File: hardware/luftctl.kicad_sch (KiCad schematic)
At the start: 41 parts, among them J1 USB_C_Receptacle_USB2.0, J2 UART, J3 I2C, J4 PWM Fan, J5 PWM Fan, SW1 Reset, U1 LMR62014XMF, U2 MIC5504-3.3YM5, U3 USBLC6-4SC6, U4 ESP32-C3-WROOM-02

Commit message: Add USB-C PD 12V input + GPIO breakout header (routed board + fab files)
Two hardware modifications to luftctl:

1. Power the fans from 12V negotiated over USB-C Power Delivery instead of
   boosting 5V on-board. Removes the boost (U1 LMR62014), its inductor,
   Schottky, feedback divider and the 5.1k CC pull-downs; adds a CH224K PD
   trigger (U5) and an LMR51420 buck (U6, 12V->3V3) for logic. The +5V rail is
   merged into +12V and the J2/J3 connector power pins move to +3V3.
2. Break out spare GPIOs on a 2.54mm Dupont header (J6): IO2, IO3 (freed from
   the removed 12V-enable), IO8, UART TX/RX, plus 3V3 and GND.

Schematic (luftctl.kicad_sch) updated and netlist-verified. A fully placed and
autorouted board is provided as luftctl-modified.kicad_pcb (board enlarged for
the new section + header; solid B.Cu ground plane; 0 unrouted, 0 clearance
violations). Firmware (main.py, esphome/luftctl.yaml) drops the 12V-enable.

JLCPCB assembly outputs (gerbers, drill, BOM, rotation-corrected CPL) for both
the original and modified boards are in hardware/jlcpcb/, with parts verified
in-stock against the jlcparts database. See hardware/MODIFICATIONS.md for the
full change spec, part selection, and the datasheet values still to confirm
(CH224K CFG straps for 12V; buck feedback divider).

Co-Authored-By: Claude Opus 4.8 (1M context) <noreply@anthropic.com>
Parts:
- removed C6: 220pF, Capacitor_SMD:C_0805_2012Metric_Pad1.18x1.45mm_HandSolder, symbol Device:C_Small
- removed D1: 1N5819, Diode_SMD:D_SOD-123, symbol Device:D_Schottky_Small
- removed L1: 10µH, Inductor_SMD:L_Bourns_SRN6045TA, symbol Device:L_Small
- removed R1: 113kΩ, Resistor_SMD:R_0805_2012Metric_Pad1.20x1.40mm_HandSolder, symbol Device:R_Small
- removed R2: 13kΩ, Resistor_SMD:R_0805_2012Metric_Pad1.20x1.40mm_HandSolder, symbol Device:R_Small
- removed R4, R5: 5.1kΩ, Resistor_SMD:R_0805_2012Metric_Pad1.20x1.40mm_HandSolder, symbol Device:R_Small
- removed U1: LMR62014XMF, Package_TO_SOT_SMD:SOT-23-5, symbol Regulator_Switching:LMR62014XMF
- removed U2: MIC5504-3.3YM5, Package_TO_SOT_SMD:SOT-23-5, symbol Regulator_Linear:MIC5504-3.3YM5
- added C12: 100nF, Capacitor_SMD:C_0805_2012Metric_Pad1.18x1.45mm_HandSolder, symbol Device:C_Small
- added C13: 10µF, Capacitor_SMD:C_0805_2012Metric_Pad1.18x1.45mm_HandSolder, symbol Device:C_Small
- added C14: 22µF, Capacitor_SMD:C_0805_2012Metric_Pad1.18x1.45mm_HandSolder, symbol Device:C_Small
- added C15: 1µF, Capacitor_SMD:C_0805_2012Metric_Pad1.18x1.45mm_HandSolder, symbol Device:C_Small
- added J6: Conn_01x08, Connector_PinHeader_2.54mm:PinHeader_1x08_P2.54mm_Vertical, symbol Connector_Generic:Conn_01x08
- added L2: 10µH, Inductor_SMD:L_Bourns_SRN6045TA, symbol Device:L_Small
- added R11: 100kΩ, Resistor_SMD:R_0805_2012Metric_Pad1.20x1.40mm_HandSolder, symbol Device:R_Small
- added R12: 22kΩ, Resistor_SMD:R_0805_2012Metric_Pad1.20x1.40mm_HandSolder, symbol Device:R_Small
- added R13, R14, R15: 0Ω, Resistor_SMD:R_0805_2012Metric_Pad1.20x1.40mm_HandSolder, symbol Device:R_Small
- added U5: CH224K, Package_SO:SSOP-10-1EP_3.9x4.9mm_P1mm_EP2.1x3.3mm, symbol Interface_USB:CH224K
- added U6: LMR51420YFDDCR, Package_TO_SOT_SMD:SOT-23-6, symbol Regulator_Switching:LMR51430
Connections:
- net +12V: now also C1.2, C3.2, C5.2, C7.2, FB1.2, TP2.1, C13.1, U6.3 (VIN), U6.5 (EN)
- net +3V3: now also J2.2 (Pin_2), J3.2 (Pin_2), C14.1, J6.1 (Pin_1), L2.2, R11.1
- net CC1: now also U5.7 (CC1)
- net CC2: now also U5.6 (CC2)
- net GND: now also C13.2, C14.2, C15.2, J6.2 (Pin_2), J6.8 (Pin_8), R12.2, R13.2, R14.2, R15.2, U5.11 (GND), U6.1 (GND)
- net GPIO2: now also J6.3 (Pin_3)
- net GPIO8: now also J6.5 (Pin_5)
- net RXD: now also J6.6 (Pin_6)
- net TXD: now also J6.7 (Pin_7)
- net VBUS: now also U5.8 (VBUS)
- removed net +5V: C1.2, C3.2, C5.2, C7.2, FB1.2, J2.2 (Pin_2), J3.2 (Pin_2), TP2.1
- net 12V_EN renamed GPIO3
- net GPIO3: now also J6.4 (Pin_4)
- new net BST_BUCK: C12.1, U6.6 (CB)
- new net CFG1: R13.1, U5.9 (CFG1)
- new net CFG2: R14.1, U5.2 (CFG2)
- new net CFG3: R15.1, U5.3 (CFG3)
- new net FB_BUCK: R11.2, R12.1, U6.4 (FB)
- new net SW_BUCK: C12.2, L2.1, U6.2 (SW)
- new net VDD_CH: C15.1, U5.1 (VDD)
- no-connect marks 2 -> 5

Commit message: CH224K: fix 12V CFG straps + VDD supply per datasheet; re-route
Datasheet research (WCH CH224 V2.0; TI LMR51420 SLUSEF6C), cross-verified,
corrected two bugs in the CH224K PD-trigger wiring that would have made the
board negotiate 9V with an unpowered controller:

- CFG3 must be pulled HIGH (to VDD) for 12V, not strapped to GND. CH224K has no
  internal CFG pull-ups, so R15 is changed from a 0R GND strap to a 10k pull-up
  to VDD (R15/CFG3 -> VDD_CH). CFG1/CFG2 stay strapped to GND (R13/R14 = 0R):
  CFG1,CFG2,CFG3 = 0,0,1 = 12V.
- VDD (pin 1) needs a series feed from VBUS; add R16 = 1k (VBUS -> VDD_CH) with
  the existing C15 1uF bypass. Previously VDD only had the cap (never powered).

LMR51420 3.3V buck confirmed correct as-is: VREF = 0.6V, R11/R12 = 100k/22k ->
3.327V (in tolerance; TI's exact pair is 100k/22.1k), no feedforward cap.

Board re-synced and re-routed with the corrections (0 unrouted, 0 clearance
violations; remaining DRC items are pre-existing footprint/silk/test-point
issues from the original board). Stale "5V" connector silk corrected to 3V3.
Assembly BOM/CPL and gerbers regenerated (19/27 lines with in-stock LCSC; new
R16 1k = C6654733). Datasheet-confirmed values documented in MODIFICATIONS.md.

Co-Authored-By: Claude Opus 4.8 (1M context) <noreply@anthropic.com>
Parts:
- added R16: 1kΩ, Resistor_SMD:R_0805_2012Metric_Pad1.20x1.40mm_HandSolder, symbol Device:R_Small
- R15: value 0Ω -> 10kΩ
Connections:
- net GND: no longer R15.2
- net VBUS: now also R16.1
- net VDD_CH: now also R15.2, R16.2
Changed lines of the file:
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@@
       (effects (font (size 1.27 1.27)) (justify left))
     )
-    (property "Value" "0Ω" (id 1) (at 62.53 200.89 0)
+    (property "Value" "10kΩ" (id 1) (at 62.53 200.89 0)
       (effects (font (size 1.27 1.27)) (justify left))
     )
@@
     )
   )
-  (global_label "GND" (shape input) (at 49.53 201.93 180) (fields_autoplaced)
+  (global_label "VDD_CH" (shape input) (at 49.53 201.93 180) (fields_autoplaced)
     (effects (font (size 1.27 1.27)) (justify right))
     (property "Intersheet References" "${INTERSHEET_REFS}" (id 0) (at 48.53 201.93 0)
@@
     )
   )
+  (symbol (lib_id "Device:R_Small") (at 25.0 210.0 0) (unit 1)
+    (in_bom yes) (on_board yes)
+    (property "Reference" "R16" (id 0) (at 38.0 209.0 0)
+      (effects (font (size 1.27 1.27)) (justify left))
+    )
+    (property "Value" "1kΩ" (id 1) (at 38.0 211.5 0)
+      (effects (font (size 1.27 1.27)) (justify left))
+    )
+    (property "Footprint" "Resistor_SMD:R_0805_2012Metric_Pad1.20x1.40mm_HandSolder" (id 2) (at 25.0 210.0 0)
+      (effects (font (size 1.27 1.27)) hide)
+    )
+    (property "Datasheet" "~" (id 3) (at 25.0 210.0 0)
+      (effects (font (size 1.27 1.27)) hide)
+    )
+    (pin "1")
+    (pin "2")
+  )
+  (global_label "VBUS" (shape input) (at 25.0 207.46 180) (fields_autoplaced)
+    (effects (font (size 1.27 1.27)) (justify right))
+    (property "Intersheet References" "${INTERSHEET_REFS}" (id 0) (at 24.0 207.46 0)
+      (effects (font (size 1.27 1.27)) (justify right) hide)
+    )
+  )
+  (global_label "VDD_CH" (shape input) (at 25.0 212.54 180) (fields_autoplaced)
+    (effects (font (size 1.27 1.27)) (justify right))
+    (property "Intersheet References" "${INTERSHEET_REFS}" (id 0) (at 24.0 212.54 0)
+      (effects (font (size 1.27 1.27)) (justify right) hide)
+    )
+  )
   (sheet_instances
     (path "/" (page "1"))
   )
   (symbol_instances
+    (path "/316fea75-6e6f-4ff4-a736-0f686100b6ba"
+      (reference "R16") (unit 1) (value "1kΩ") (footprint "Resistor_SMD:R_0805_2012Metric_Pad1.20x1.40mm_HandSolder")
+    )
     (path "/347cbe5d-4fbb-48f2-9d2e-05896824e8fe"
       (reference "U5") (unit 1) (value "CH224K") (footprint "Package_SO:SSOP-10-1EP_3.9x4.9mm_P1mm_EP2.1x3.3mm")
@@
     )
     (path "/1a14d875-78ee-4707-afc7-6f65a6ad48c0"
-      (reference "R15") (unit 1) (value "0Ω") (footprint "Resistor_SMD:R_0805_2012Metric_Pad1.20x1.40mm_HandSolder")
+      (reference "R15") (unit 1) (value "10kΩ") (footprint "Resistor_SMD:R_0805_2012Metric_Pad1.20x1.40mm_HandSolder")
     )
     (path "/21ca11bb-5260-4772-98da-6ca3e72e7446"

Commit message: Fix USBLC6 on 12V VBUS, add VBUS TVS, switch to JLCPCB Basic parts
- U3 (USBLC6) pin 5 disconnected from VBUS. VBUS is 12V after PD
  negotiation and the USBLC6 supply-pin clamp conducts from ~6V. Left
  floating (not +3V3) since CC1/CC2 on U3 sit near 5V.
- Add D4 SMF15A (15V standoff) TVS from VBUS to GND, above J1.
- SW1/JP1 buttons: PTS810 -> TS-1088-AR02016 (C720477, JLCPCB Basic).
- Re-source all passives/LEDs to JLCPCB Basic parts; R9 660R -> 680R.
- U4 -> ESP32-C3-WROOM-02-N4 (C2934560, PCB antenna, in stock).
- Pin headers J4/J5/J6 dropped from the assembly BOM (hand-soldered).
- Local re-route; DRC 0 unconnected, no shorts; board matches schematic.
- MODIFICATIONS.md: sourcing notes, order plan, to-do list.

Co-Authored-By: Claude Opus 5.5 (1M context) <noreply@anthropic.com>
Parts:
- added D4: SMF15A, Diode_SMD:D_SOD-123F, symbol Device:D_Zener_Small
- JP1, SW1: footprint Button_Switch_SMD:SW_SPST_PTS810 -> Button_Switch_SMD:SW_SPST_TS-1088-xR020
- R9: value 660Ω -> 680Ω
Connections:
- net GND: now also D4.2 (A)
- net VBUS: now also D4.1 (K); no longer U3.5 (VBUS)
- no-connect marks 5 -> 6
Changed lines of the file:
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@@
   (junction (at 87.63 115.57) (diameter 0) (color 0 0 0 0)
   )
+  (no_connect (at 95.25 58.42))
   (no_connect (at 67.31 63.5))
   (no_connect (at 67.31 66.04))
@@
       (effects (font (size 1.27 1.27)) (justify left))
     )
-    (property "Value" "660Ω" (id 1) (at 176.7586 44.323 0)
+    (property "Value" "680Ω" (id 1) (at 176.7586 44.323 0)
       (effects (font (size 1.27 1.27)) (justify left))
     )
@@
       (effects (font (size 1.27 1.27)) (justify right))
     )
-    (property "Footprint" "Button_Switch_SMD:SW_SPST_PTS810" (id 2) (at 162.56 95.25 0)
+    (property "Footprint" "Button_Switch_SMD:SW_SPST_TS-1088-xR020" (id 2) (at 162.56 95.25 0)
       (effects (font (size 1.27 1.27)) hide)
     )
@@
     )
     (property "Datasheet" "" (id 3) (at 238.76 36.83 0)
-      (effects (font (size 1.27 1.27)) hide)
-    )
-    (pin "1")
-  )
-  (symbol (lib_id "power:VBUS") (at 95.25 58.42 0) (unit 1)
-    (in_bom yes) (on_board yes) (fields_autoplaced)
-    (property "Reference" "#PWR0101" (id 0) (at 95.25 62.23 0)
-      (effects (font (size 1.27 1.27)) hide)
-    )
-    (property "Value" "VBUS" (id 1) (at 95.25 53.34 0))
-    (property "Footprint" "" (id 2) (at 95.25 58.42 0)
-      (effects (font (size 1.27 1.27)) hide)
-    )
-    (property "Datasheet" "" (id 3) (at 95.25 58.42 0)
       (effects (font (size 1.27 1.27)) hide)
     )
@@
       (effects (font (size 1.27 1.27)) (justify left))
     )
-    (property "Footprint" "Button_Switch_SMD:SW_SPST_PTS810" (id 2) (at 146.05 95.25 0)
+    (property "Footprint" "Button_Switch_SMD:SW_SPST_TS-1088-xR020" (id 2) (at 146.05 95.25 0)
       (effects (font (size 1.27 1.27)) hide)
     )
@@
     )
   )
+  (symbol (lib_id "Device:D_Zener_Small") (at 250.19 180.34 0) (unit 1)
+    (in_bom yes) (on_board yes)
+    (property "Reference" "D4" (id 0) (at 248.92 177.8 0)
+      (effects (font (size 1.27 1.27)) (justify left))
+    )
+    (property "Value" "SMF15A" (id 1) (at 247.65 182.88 0)
+      (effects (font (size 1.27 1.27)) (justify left))
+    )
+    (property "Footprint" "Diode_SMD:D_SOD-123F" (id 2) (at 250.19 180.34 90)
+      (effects (font (size 1.27 1.27)) hide)
+    )
+    (property "Datasheet" "~" (id 3) (at 250.19 180.34 90)
+      (effects (font (size 1.27 1.27)) hide)
+    )
+    (pin "1")
+    (pin "2")
+  )
+  (symbol (lib_id "power:VBUS") (at 247.65 180.34 0) (unit 1)
+    (in_bom yes) (on_board yes) (fields_autoplaced)
+    (property "Reference" "#PWR0105" (id 0) (at 247.65 184.15 0)
+      (effects (font (size 1.27 1.27)) hide)
+    )
+    (property "Value" "VBUS" (id 1) (at 247.65 175.26 0))
+    (property "Footprint" "" (id 2) (at 247.65 180.34 0)
+      (effects (font (size 1.27 1.27)) hide)
+    )
+    (property "Datasheet" "" (id 3) (at 247.65 180.34 0)
+      (effects (font (size 1.27 1.27)) hide)
+    )
+    (pin "1")
+  )
+  (symbol (lib_id "power:GND") (at 252.73 180.34 0) (unit 1)
+    (in_bom yes) (on_board yes) (fields_autoplaced)
+    (property "Reference" "#PWR0106" (id 0) (at 252.73 184.15 0)
+      (effects (font (size 1.27 1.27)) hide)
+    )
+    (property "Value" "GND" (id 1) (at 252.73 185.42000000000002 0))
+    (property "Footprint" "" (id 2) (at 252.73 180.34 0)
+      (effects (font (size 1.27 1.27)) hide)
+    )
+    (property "Datasheet" "" (id 3) (at 252.73 180.34 0)
+      (effects (font (size 1.27 1.27)) hide)
+    )
+    (pin "1")
+  )
   (sheet_instances
     (path "/" (page "1"))
   )
   (symbol_instances
+    (path "/371ed725-b348-462b-98a2-1bc40e20266f"
+      (reference "D4") (unit 1) (value "SMF15A") (footprint "Diode_SMD:D_SOD-123F")
+    )
+    (path "/5f549bb8-e2a5-4695-a0c0-1e251555ddb7"
+      (reference "#PWR0105") (unit 1) (value "VBUS") (footprint "")
+    )
+    (path "/426ef3c8-2397-43bd-8c5a-30a016926c4c"
+      (reference "#PWR0106") (unit 1) (value "GND") (footprint "")
+    )
     (path "/316fea75-6e6f-4ff4-a736-0f686100b6ba"
       (reference "R16") (unit 1) (value "1kΩ") (footprint "Resistor_SMD:R_0805_2012Metric_Pad1.20x1.40mm_HandSolder")
@@
       (reference "#PWR045") (unit 1) (value "GND") (footprint "")
     )
-    (path "/56ccb014-0b3a-4ed5-a9d0-c70f892a18b4"
-      (reference "#PWR0101") (unit 1) (value "VBUS") (footprint "")
-    )
     (path "/b7842966-8df3-4cf3-9777-c4e60f800cac"
       (reference "#PWR0102") (unit 1) (value "VBUS") (footprint "")
@@
     )
     (path "/a6ee9dc5-ab2b-4518-bb5c-e8a7ad56c775"
-      (reference "JP1") (unit 1) (value "Bootloader") (footprint "Button_Switch_SMD:SW_SPST_PTS810")
+      (reference "JP1") (unit 1) (value "Bootloader") (footprint "Button_Switch_SMD:SW_SPST_TS-1088-xR020")
     )
     (path "/1bb2bd4c-d169-4efd-b5f4-929647c923af"
@@
     )
     (path "/00000000-0000-0000-0000-00005f25bf97"
-      (reference "R9") (unit 1) (value "660Ω") (footprint "Resistor_SMD:R_0805_2012Metric_Pad1.20x1.40mm_HandSolder")
+      (reference "R9") (unit 1) (value "680Ω") (footprint "Resistor_SMD:R_0805_2012Metric_Pad1.20x1.40mm_HandSolder")
     )
     (path "/00000000-0000-0000-0000-00005f23560c"
@@
     )
     (path "/4f7ea4a8-8301-4901-932a-b6880e260ab7"
-      (reference "SW1") (unit 1) (value "Reset") (footprint "Button_Switch_SMD:SW_SPST_PTS810")
+      (reference "SW1") (unit 1) (value "Reset") (footprint "Button_Switch_SMD:SW_SPST_TS-1088-xR020")
     )
     (path "/e2205131-398e-4b23-a7cb-6ed24a167152"

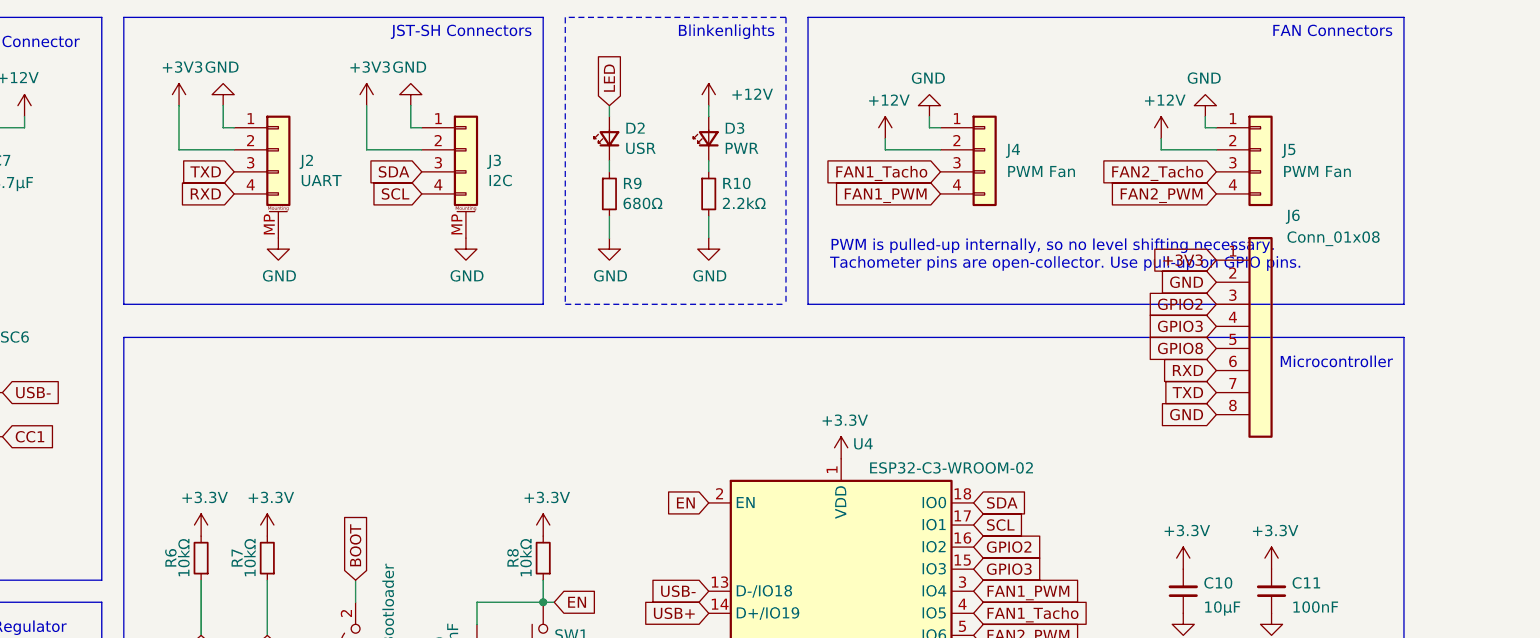
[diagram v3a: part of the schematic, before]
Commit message: Remove J2/J3 JST-SH connectors; J6 becomes 1x10 with SDA/SCL and pin labels
UART was already on J6 and flashing/logs go over native USB, so J2 was
redundant. SDA (GPIO0) and SCL (GPIO1) move from J3 to J6 pins 9/10.
J6: 3V3, GND, IO2, IO3, IO8, RX, TX, GND, SDA, SCL, labelled on silk.
Local re-route; DRC 0 unconnected, no new violations; board matches
schematic. Drops the C160404 Extended line from the BOM.

Co-Authored-By: Claude Opus 5.5 (1M context) <noreply@anthropic.com>
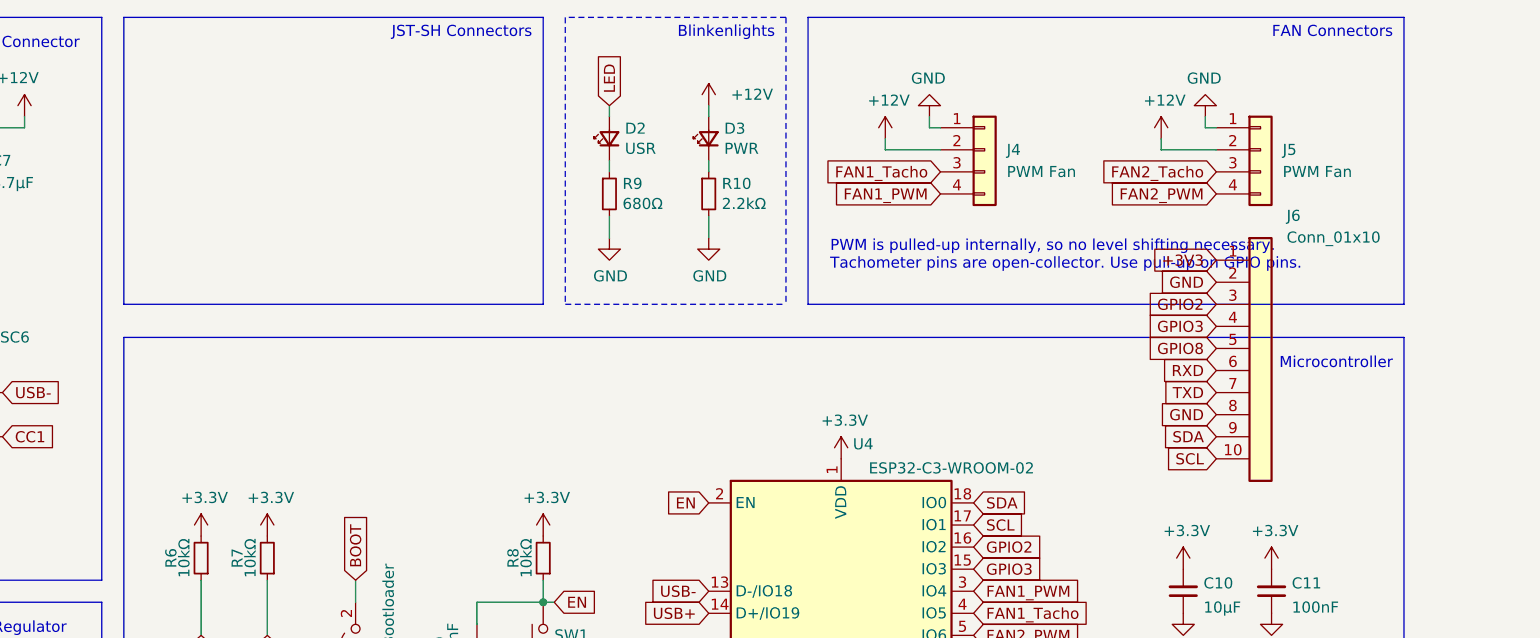
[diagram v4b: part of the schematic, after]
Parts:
- removed J2: UART, Connector_JST:JST_SH_SM04B-SRSS-TB_1x04-1MP_P1.00mm_Horizontal, symbol Connector_Generic_MountingPin:Conn_01x04_MountingPin
- removed J3: I2C, Connector_JST:JST_SH_SM04B-SRSS-TB_1x04-1MP_P1.00mm_Horizontal, symbol Connector_Generic_MountingPin:Conn_01x04_MountingPin
- J6: value Conn_01x08 -> Conn_01x10; footprint Connector_PinHeader_2.54mm:PinHeader_1x08_P2.54mm_Vertical -> Connector_PinHeader_2.54mm:PinHeader_1x10_P2.54mm_Vertical; symbol Connector_Generic:Conn_01x08 -> Connector_Generic:Conn_01x10
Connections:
- net SCL: now also J6.10 (Pin_10)
- net SDA: now also J6.9 (Pin_9)
